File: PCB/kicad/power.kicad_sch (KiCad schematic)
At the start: 23 parts

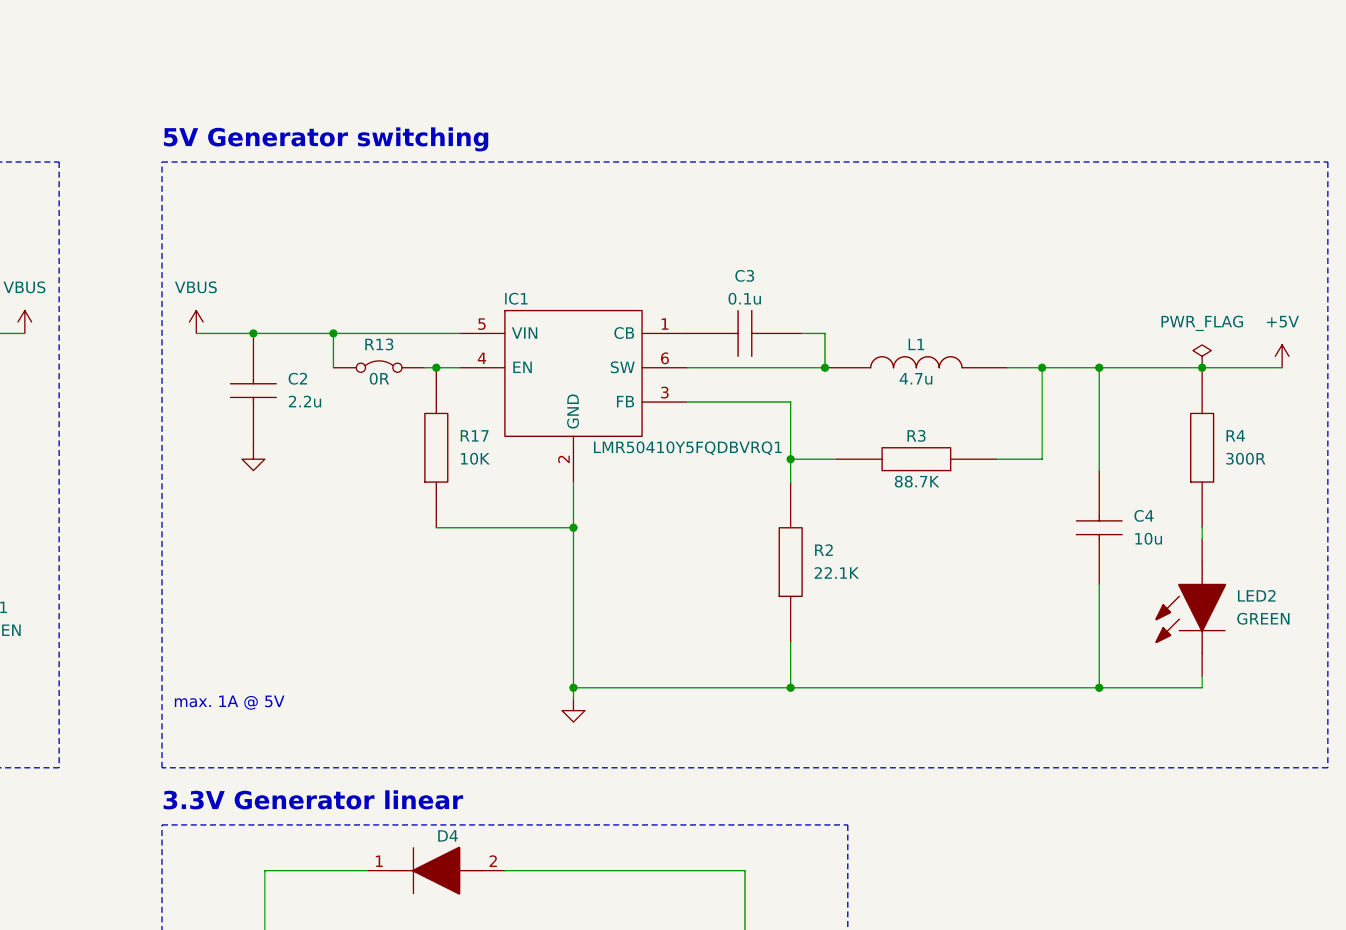
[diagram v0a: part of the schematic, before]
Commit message: PCB 1.0: - Corrected 5V generation - Corrected USB ESD protection - Replaced USB type-C with micro type-B
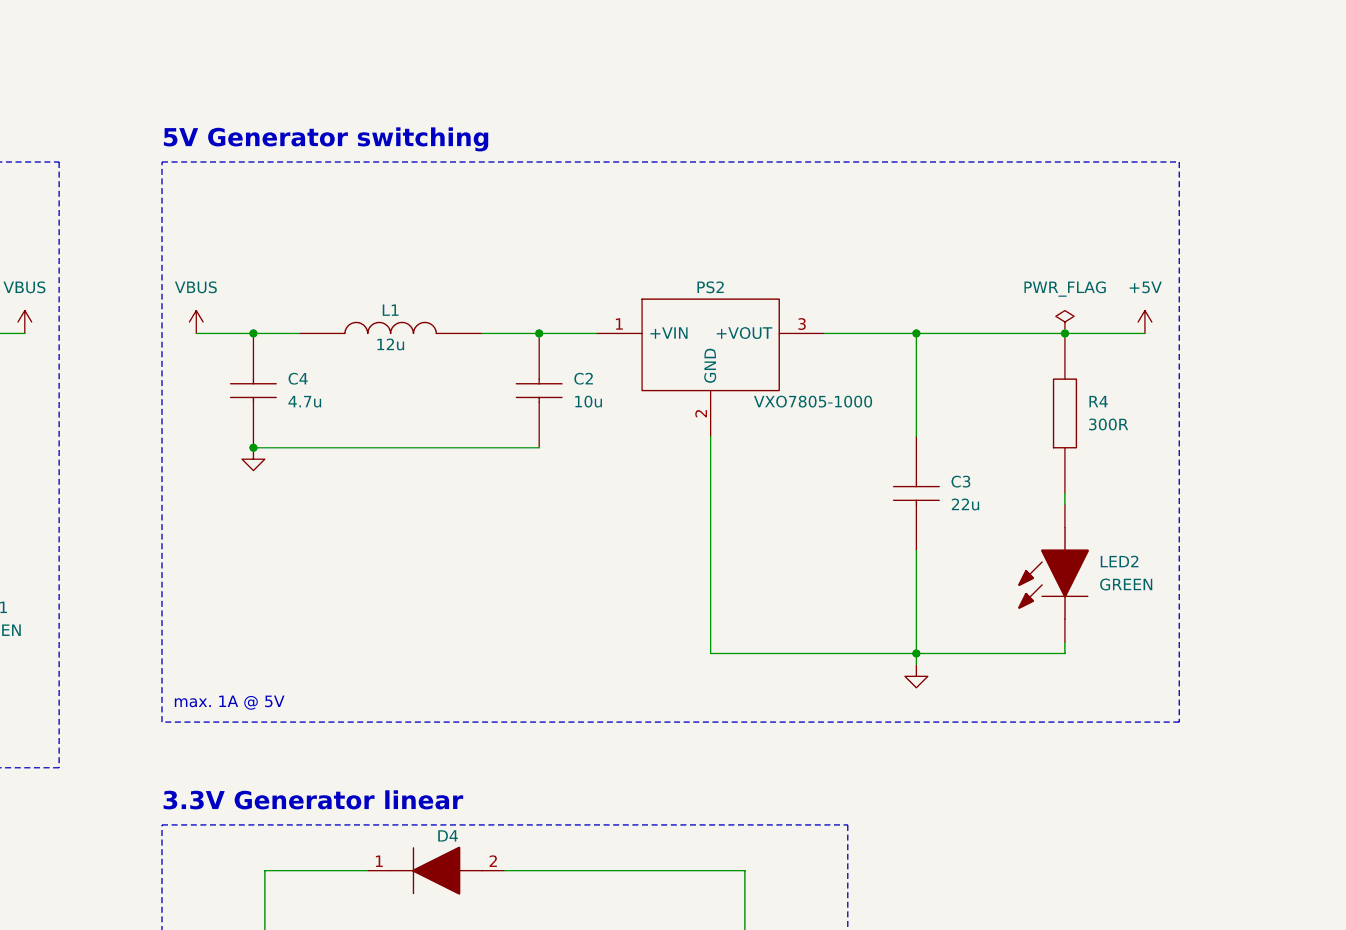
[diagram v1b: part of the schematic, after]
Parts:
- removed C2: 2.2u, alecot:CAPC3116X180N, symbol alecot:GCM31CR71H225KA55K
- removed C3: 0.1u, alecot:CAPC1005X55N, symbol alecot:GRM155R61H104KE19D
- removed C4: 10u, alecot:CAPC3225X270N, symbol alecot:GRM32ER71H106KA12L
- removed IC1: ~, alecot:SOT95P280X145-6N, symbol alecot:LMR50410Y5FQDBVRQ1
- removed L1: 4.7u, alecot:LQM21PHR47NG0D, symbol alecot:LQM21PN4R7MGHL
- removed R13: 0R, alecot:ERJ3EKF1000V, symbol alecot:ERJ-3GEY0R00V
- removed R17: 10K, alecot:RESC1608X55N, symbol alecot:ERJ-3EKF1002V
- removed R2: 22.1K, alecot:RESC1608X55N, symbol alecot:ERJ-3EKF2212V
- removed R3: 88.7K, alecot:RESC1608X55N, symbol alecot:ERJ-3EKF8872V
- added C2: 10u, alecot:CAPC3225X270N, symbol alecot:GRM32ER71H106KA12L
- added C3: 22u, CAPC1608X90N, symbol alecot:GRM188R61A226ME15D
- added C4: 4.7u, CAPC2012X135N, symbol alecot:GRT21BR61H475KE13L
- added L1: 12u, 1227ASH100MP2, symbol alecot:1227AS-H-120M=P2
- added PS2: VXO7805-1000, VXO780121000, symbol alecot:VXO7805-1000
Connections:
- net +5V: now also C3.2, PS2.3 (+VOUT)
- net GND: now also C2.1, C3.1, C4.1, PS2.2 (GND)
- net VBUS: now also C4.2, L1.1
- new net: C2.2, L1.2, PS2.1 (+VIN)
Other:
- moved on the sheet: LED2, R4

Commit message: Added some test points
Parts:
- C3: footprint CAPC1608X90N -> alecot:CAPC1608X90N
- C4: footprint CAPC2012X135N -> alecot:CAPC2012X135N
- L1: footprint 1227ASH100MP2 -> alecot:1227ASH100MP2
- PS2: footprint VXO780121000 -> alecot:VXO780121000
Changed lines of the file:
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@@
       (effects (font (size 1.27 1.27)))
     )
-    (property "Footprint" "1227ASH100MP2" (at 194.31 46.99 0)
+    (property "Footprint" "alecot:1227ASH100MP2" (at 194.31 46.99 0)
       (effects (font (size 1.27 1.27)) (justify left) hide)
     )
@@
       (effects (font (size 1.27 1.27)) (justify left) hide)
     )
-    (property "Footprint" "VXO780121000" (at 226.06 45.72 0)
+    (property "Footprint" "alecot:VXO780121000" (at 226.06 45.72 0)
       (effects (font (size 1.27 1.27)) (justify left) hide)
     )
@@
       (effects (font (size 1.27 1.27)) (justify right))
     )
-    (property "Footprint" "CAPC2012X135N" (at 153.67 39.37 0)
+    (property "Footprint" "alecot:CAPC2012X135N" (at 153.67 39.37 0)
       (effects (font (size 1.27 1.27)) (justify left) hide)
     )
@@
       (effects (font (size 1.27 1.27)) (justify right))
     )
-    (property "Footprint" "CAPC1608X90N" (at 227.33 52.07 0)
+    (property "Footprint" "alecot:CAPC1608X90N" (at 227.33 52.07 0)
       (effects (font (size 1.27 1.27)) (justify left) hide)
     )
